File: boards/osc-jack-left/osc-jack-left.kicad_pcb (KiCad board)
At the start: 6 copper layers, 172.5 x 144 mm, 1099 parts, among them J1001 WQP518MA, J1002 WQP518MA, J1003 WQP518MA, J1004 WQP518MA, J1005 WQP518MA, J1006 WQP518MA, J1007 WQP518MA, J1008 WQP518MA, J1009 WQP518MA, J101 WQP518MA, J1010 WQP518MA, J102 WQP518MA, J103 WQP518MA, J104 WQP518MA, J105 WQP518MA, J106 WQP518MA, J107 WQP518MA, J108 WQP518MA, J109 WQP518MA, J110 WQP518MA, J201 WQP518MA, J202 WQP518MA, J203 WQP518MA, J204 WQP518MA, J205 WQP518MA, J206 WQP518MA, J207 WQP518MA, J208 WQP518MA, J209 WQP518MA, J210 WQP518MA, J301 WQP518MA, J302 WQP518MA, J303 WQP518MA, J304 WQP518MA, J305 WQP518MA, J306 WQP518MA, J307 WQP518MA, J308 WQP518MA, J309 WQP518MA, J310 WQP518MA, J401 WQP518MA, J402 WQP518MA, J403 WQP518MA, J404 WQP518MA, J405 WQP518MA, J406 WQP518MA, J407 WQP518MA, J408 WQP518MA, J409 WQP518MA, J410 WQP518MA, J501 WQP518MA, J502 WQP518MA, J503 WQP518MA, J504 WQP518MA, J505 WQP518MA, J506 WQP518MA, J507 WQP518MA, J508 WQP518MA, J509 WQP518MA, J510 WQP518MA, J601 WQP518MA, J602 WQP518MA, J603 WQP518MA, J604 WQP518MA, J605 WQP518MA, J606 WQP518MA, J607 WQP518MA, J608 WQP518MA, J609 WQP518MA, J610 WQP518MA, J701 WQP518MA, J702 WQP518MA, J703 WQP518MA, J704 WQP518MA, J705 WQP518MA, J706 WQP518MA, J707 WQP518MA, J708 WQP518MA, J709 WQP518MA, J710 WQP518MA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

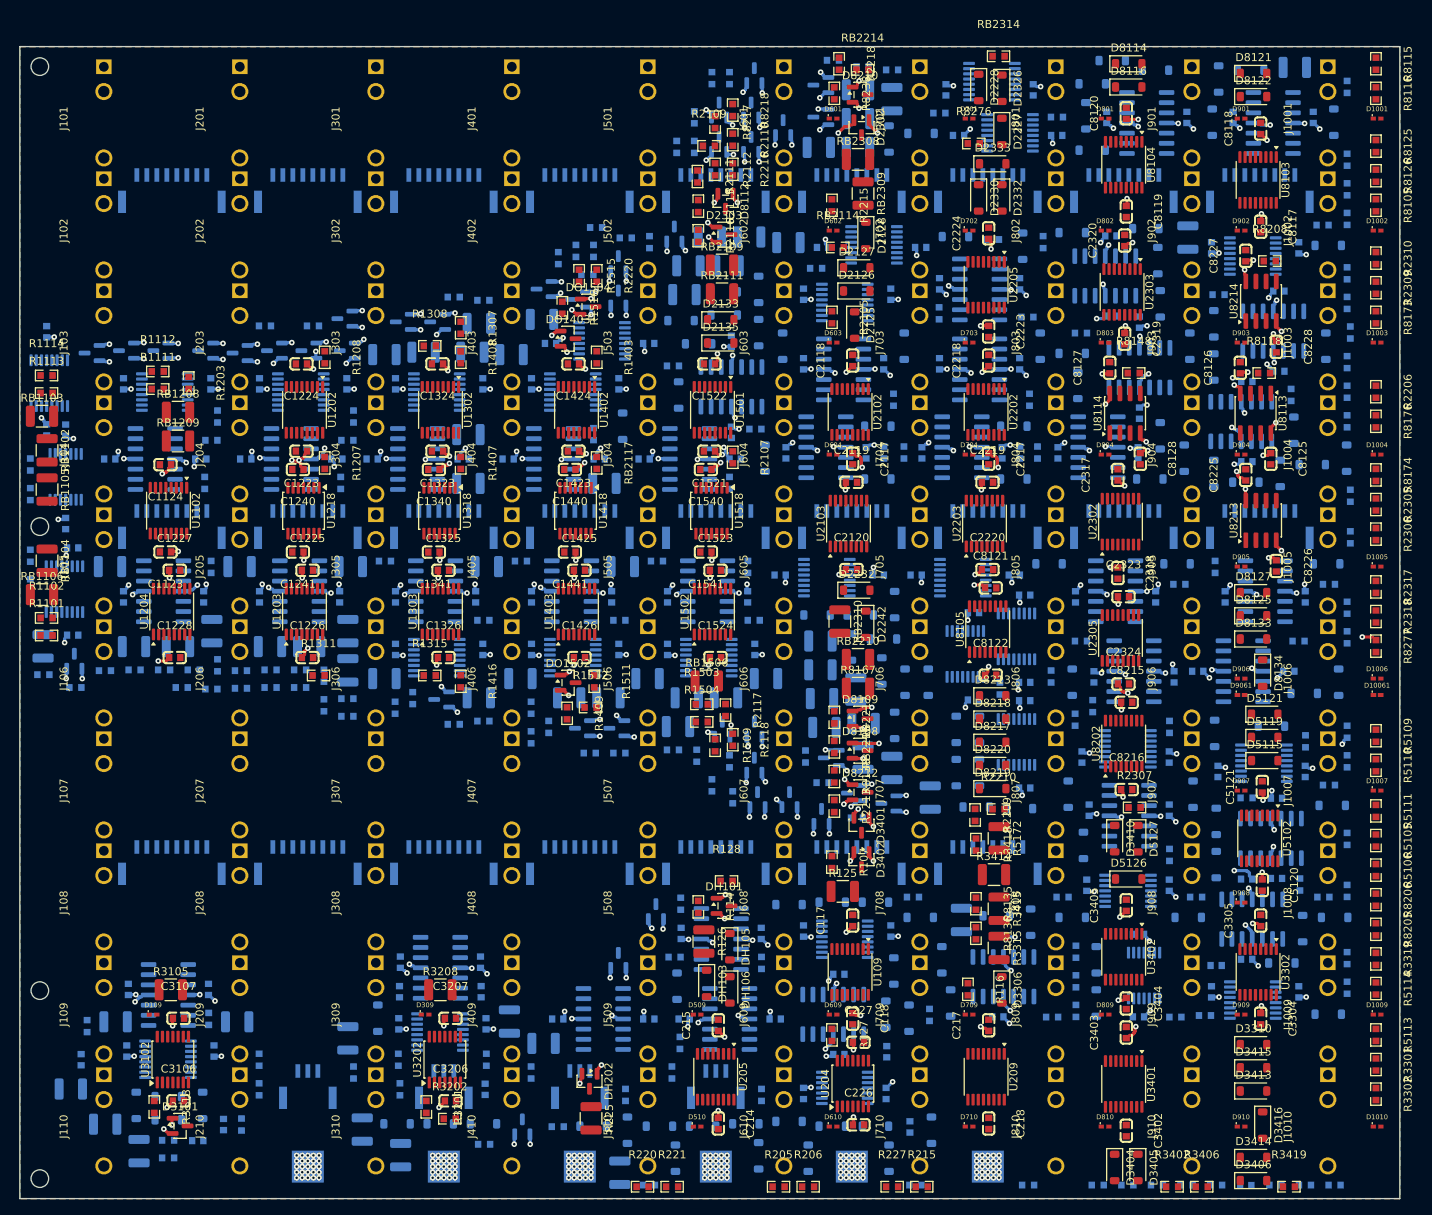
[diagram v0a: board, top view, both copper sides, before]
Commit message: Route osc-jack-left on CI: stage rail-links, open edges 1423 -> 1361
Adopted grid-routing stage pushed as soon as it was promoted.
Unvalidated draft; electrical and physical qualification NOT RUN.

Run: https://github.com/Takazudo/zudo-osc-hole-field/actions/runs/37351839421
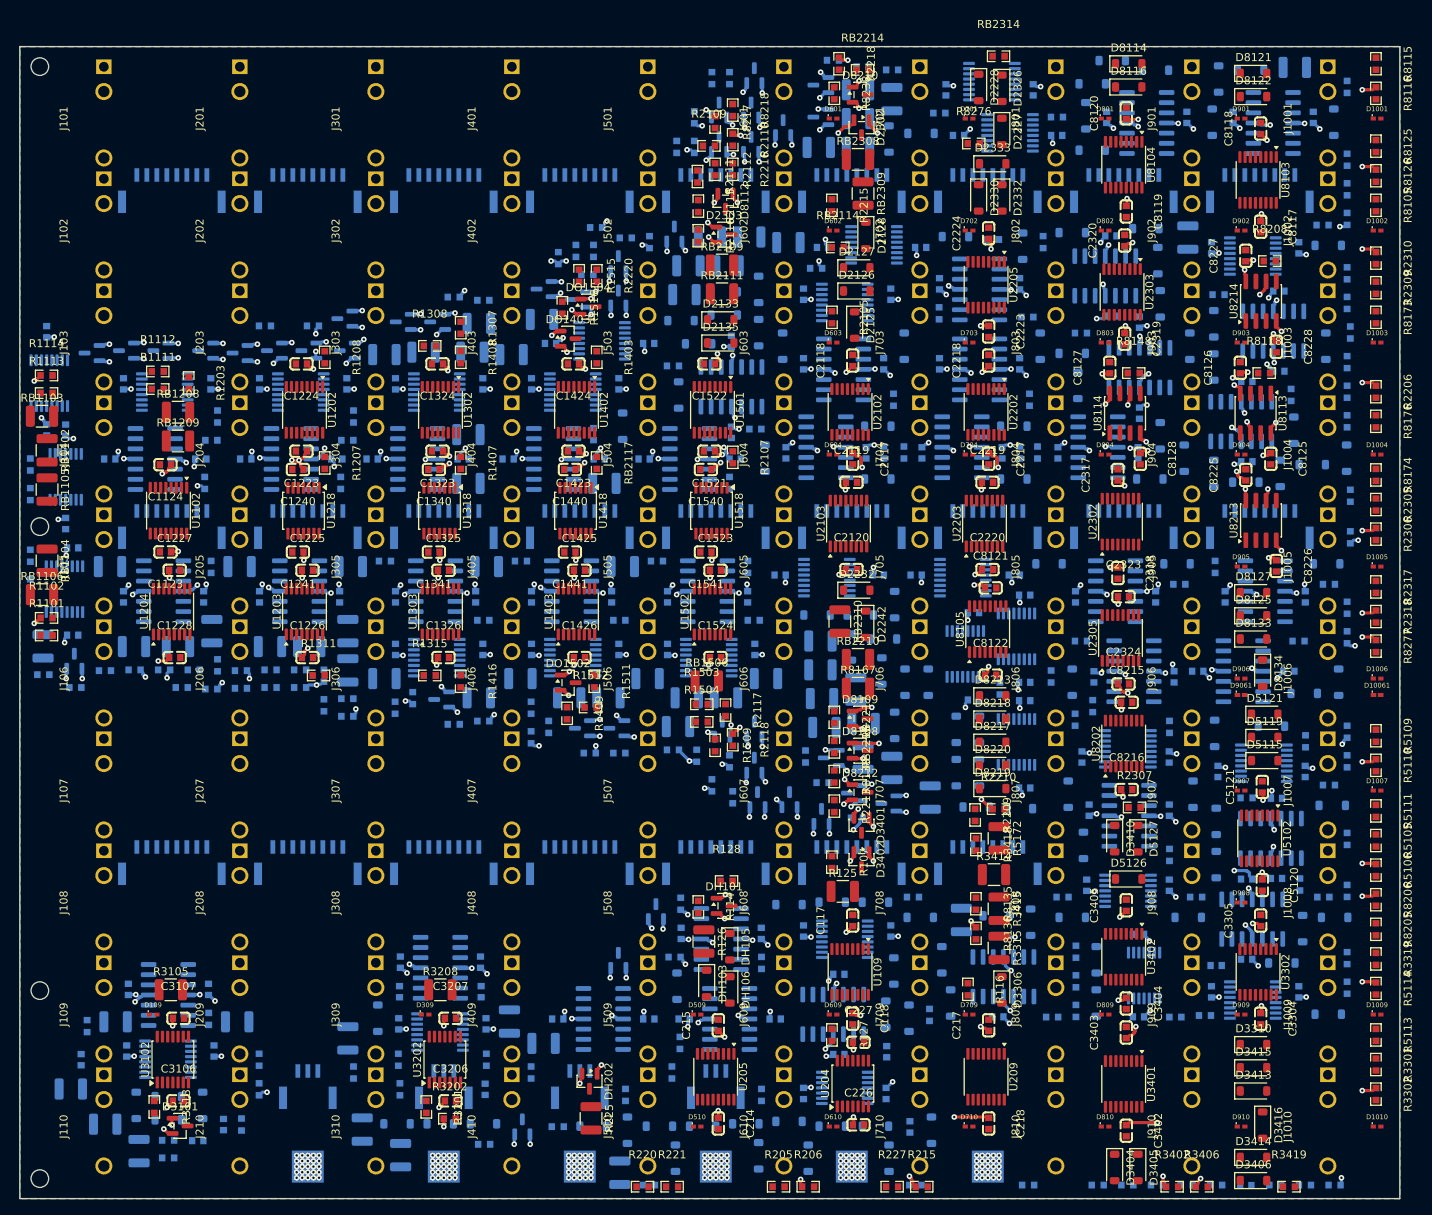
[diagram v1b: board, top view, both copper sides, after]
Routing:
- net +5V: track 0.00 -> 990.8 mm, vias 25 -> 83
- net +12V: track 125.7 -> 163.9 mm, vias 227 -> 229
